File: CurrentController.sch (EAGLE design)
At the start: 136 parts, among them CN1 220uF, CN3 47uF, IC1 LM340S-12, IC2 L7912, IC3 TS514, IC4 MIC5205-5V, IC5 MEGA8-AI, IC6 MIC5205-3V, IC7 PMOS-SOT323, IC8 PMOS-SOT323-SC89, T1 100k, U1 TPS7A470, U2 AD8676, U3 AD8676, U4 NT2006

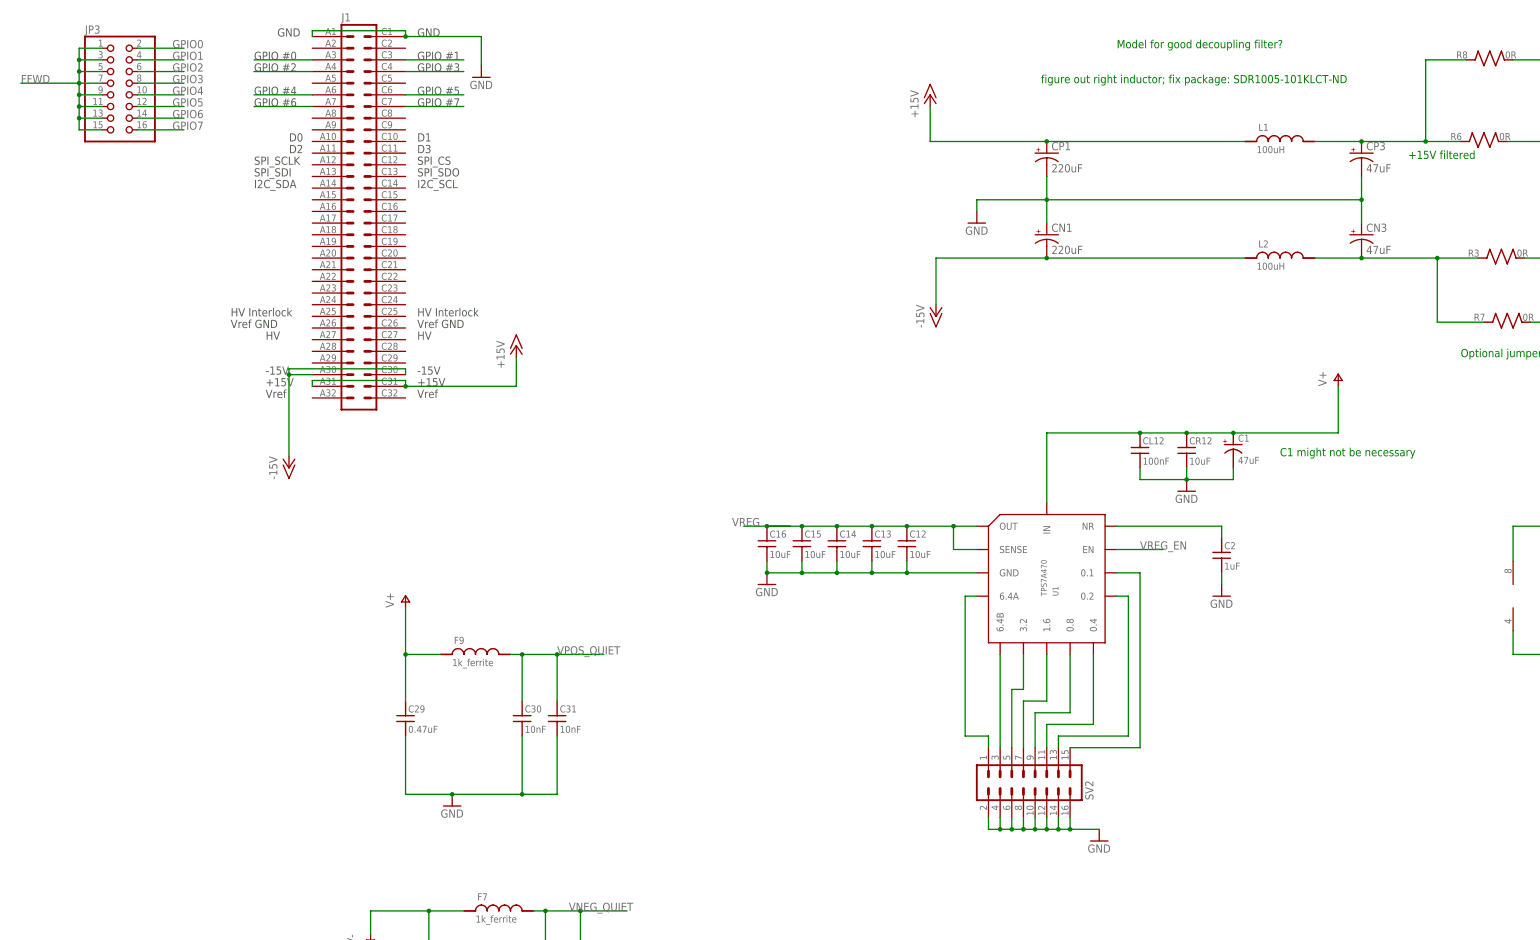
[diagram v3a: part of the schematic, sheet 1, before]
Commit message: Updated silkscreen; other minor mods
Prepping for fabrication at macrofab.
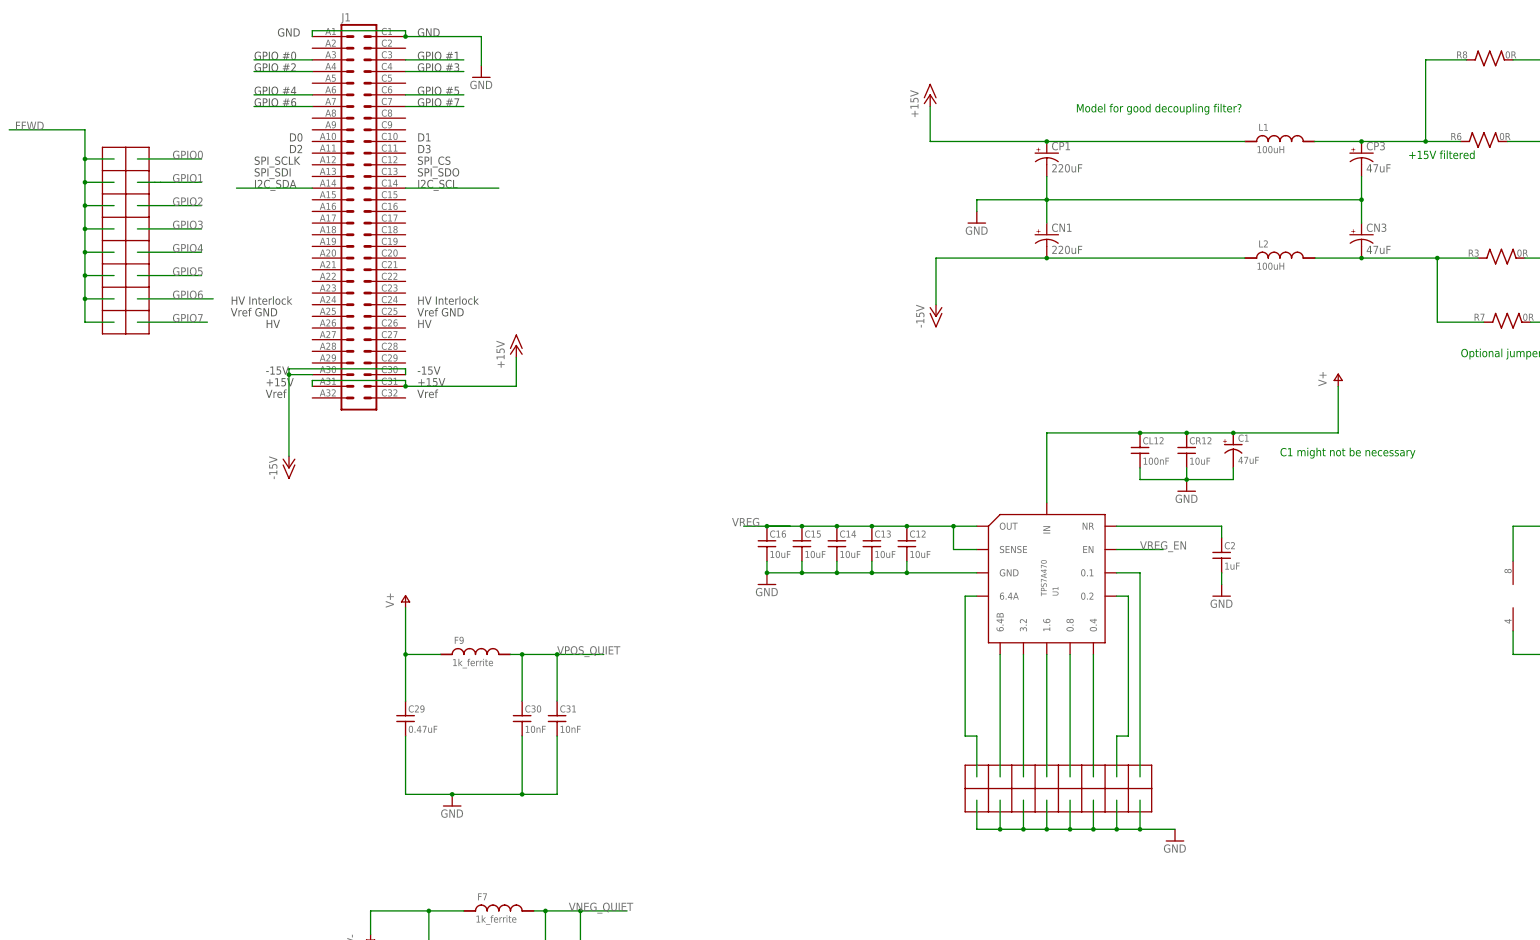
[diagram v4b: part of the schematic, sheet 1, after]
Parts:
- removed JP2: (no value), pinhead:PINHD-1X3
- removed JP3: (no value), pinhead:PINHD-2X8
- removed L3: (no value), jqi_passives:L_FERRITE_SMDLFERRITE_0805
- removed SV2: (no value), connector-jqi:MA08-2
- added F1: 1k_ferrite, jqi_passives:L_FERRITE_SMDLFERRITE_0603
- added J2, J3: 2X8_LOW_PROFILE_JUMPER, Eurocard-HV-piezo-driver:2X8_LOW_PROFILE_JUMPER
- added J4: 1X3_LOW_PROFILE_JUMPER, pinhead:1X3_LOW_PROFILE_JUMPER
- added JP4: 1X2_LOW_PROFILE_JUMPER, Eurocard-HV-piezo-driver:1X2_LOW_PROFILE_JUMPER
- added MR12: 1k, jqi_passives:R_SMDR0805
- added R24: 10k, jqi_passives:R_SMDR0603
- BUF, FFWD, U2, U3: PARTNO AD8676ARMZ-REELCT-ND -> AD8676ARMZ
- C10, C24, C29: PARTNO 490-4382-1-ND -> LLL31MR71E474MA01L
- C11, C21, C25, C26, C30, C31: PARTNO 478-2890-1-ND -> 03063C103KAT2A
- C12, C13, C14, C15, C16, CR12, CR3, CR4: PARTNO 1276-2890-1-ND -> CL21A106KAFN3NE
- C17, C22, C23, C27, C28, C32, C33, CD1, CD2, CL1, CL12, CL2, CL3, CL4, CL5, CL6: PARTNO 445-1316-1-ND -> C1608X7R1E104K080AA
- C18: value (none) -> 1uF; PARTNO (none) -> CL10B105KA8NNNC
- C19, C2, C20, MC1: PARTNO 1276-1184-1-ND -> CL10B105KA8NNNC
- C3: PARTNO 1276-2119-1-ND -> CL10B822KB8NNNC
- C4, C5, C6, C7, C8, C9: PARTNO 445-9112-1-ND -> C2012X5R1E226M125AC
- CN1, CP1: PARTNO PCE3955CT-ND -> EEE-1VA221UP
- CN3, CP3: PARTNO 399-3797-1-ND -> T491D476M025AT
- CUR, MOD_IN: PARTNO (none) -> 5227161-7
- D1, D2, D3, D4: PARTNO 568-7397-1-ND -> PMEG3005EB,115
- DAC1: PARTNO AD5541ARZ-ND -> AD5541BRZ
- ENC, LCD: PARTNO (none) -> 75869-132LF
- F3, F4, F7, F8, F9: PARTNO 490-1034-1-ND -> BLM18HG102SN1D
- IC1: PARTNO LM340S-12/NOPB-ND -> LM340S-12/NOPB
- IC2: PARTNO MC7912CD2TGOS-ND -> MC7912CD2TG
- IC3: PARTNO 497-4453-1-ND -> TS514AIDT
- IC4: PARTNO 576-1261-1-ND -> MIC5205-5.0YM5-TR
- IC5: PARTNO (none) -> ATMEGA328P-AU
- IC6: PARTNO 576-1258-1-ND -> MIC5205-3.0YM5-TR
- J1: PARTNO (none) -> 5650945-5
- JP1: PARTNO (none) -> 68000-406HLF
- L1, L2: device jqi_passives:L_FERRITE_SMD-CC1583 -> jqi_passives:WURTH_74477020; PARTNO MSS1583-104KEB -> 74477020
- LOUT1: PARTNO 587-3070-1-ND / DN7906CT-ND -> CBC3225T680KR
- MON: PARTNO (none) -> 1909763-1
- MON1, R2: PARTNO P100HCT-ND -> ERJ-3EKF1000V
- MR1, MR10, MR11, MR2, MR3, MR4, MR5, MR6, MR7, MR8, MR9: PARTNO P1.0KBFCT-ND -> ERA-6ARB102V
- QFB1: PARTNO NDS0605CT-ND -> *
- R1, R100, R17, R18: PARTNO P10.0KHCT-ND -> ERJ-3EKF1002V
- R10, R11, R13, R9: PARTNO 742C083103JPCT-ND -> 742C083103JP
- R12, R19, R22: PARTNO P28.7KHCT-ND -> ERJ-3EKF2872V
- R20: PARTNO (none) -> ERJ-6ENF49R9V
- R21, R23, R4, R5, R50: PARTNO P3.00KHCT-ND -> ERJ-3EKF3001V
- R25: PARTNO P200KHCT-ND -> ERJ-3EKF2003V
- R3, R6, R7, R8: PARTNO P0.0ECT-ND -> ERJ-8GEY0R00V
- R36: PARTNO P11.0KHCT-ND -> ERJ-3EKF1102V
- R37: PARTNO P7.50KHCT-ND -> ERJ-3EKF7501V
- SV1: PARTNO (none) -> 67996-406HLF
- T1: PARTNO 3006P-104LF-ND -> 3006P-1-104LF
- U$5: PARTNO (none) -> 36103205
- U1: PARTNO 296-37243-1-ND -> TPS7A4701RGWT
- U4: PARTNO 568-6661-1-ND -> NVT2006BS,118
- VREFIC: PARTNO LM399H#PBF-ND -> LM399H#PBF
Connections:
- new net N$35: JP4.P$2, R20.2
- new net SCL: IC5.PC5(ADC5/SCL), J1.C14
- new net SDA: IC5.PC4(ADC4/SDA), J1.A14
- net FEED_FWD: now also J4.P$2; no longer JP2.2
- net FFWD: now also J2.P$1, J2.P$11, J2.P$13, J2.P$15, J2.P$3, J2.P$5, J2.P$7, J2.P$9; no longer JP3.1, JP3.11, JP3.13, JP3.15, JP3.3, JP3.5, JP3.7, JP3.9
- net FFWD_POSTGAIN: now also J4.P$1; no longer JP2.3
- net GND: now also F1.2, J3.P$1, J3.P$11, J3.P$13, J3.P$15, J3.P$3, J3.P$5, J3.P$7, J3.P$9, J4.P$3, MR12.2, R24.1; no longer JP2.1, L3.2, SV2.10, SV2.12, SV2.14, SV2.16, SV2.2, SV2.4, SV2.6, SV2.8
- net GPIO0: now also J2.P$2; no longer JP3.2
- net GPIO1: now also J2.P$4; no longer JP3.4
- net GPIO2: now also J2.P$6; no longer JP3.6
- net GPIO3: now also J2.P$8; no longer JP3.8
- net GPIO4: now also J2.P$10; no longer JP3.10
- net GPIO5: now also J2.P$12; no longer JP3.12
- net GPIO6: now also J2.P$14; no longer JP3.14
- net GPIO7: now also J2.P$16; no longer JP3.16
- net MODIN_B: now also JP4.P$1, R24.2; no longer R20.2
- net N$19: now also J3.P$2; no longer SV2.1
- net N$21: now also MR12.1
- net N$27: now also J3.P$4; no longer SV2.3
- net N$31: now also J3.P$6; no longer SV2.5
- net N$34: now also J3.P$8; no longer SV2.7
- net N$39: now also J3.P$10; no longer SV2.9
- net N$41: now also J3.P$12; no longer SV2.11
- net N$43: now also J3.P$14; no longer SV2.13
- net N$44: now also J3.P$16; no longer SV2.15
- net VSS: now also F1.1; no longer L3.1
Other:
- note removed: "Use: MSS1583-104KE"
- note removed: "additional high-freq capacitor?"
- note removed: "figure out right inductor; fix package: SDR1005-101KLCT-ND"
- note removed: "switch to CoilCraft; use LC filter design tool"
- moved on the sheet: R20
